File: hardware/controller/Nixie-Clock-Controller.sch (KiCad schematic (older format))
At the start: 62 parts, among them IC1 ESP32-DEVKITC-V4, IC2 74141, J1 9/12-35V DC in, J2 Nixies-Connector, J3 Buttons, J4 Buzzer, Q1 MPSA42, Q10 MPSA42, Q11 MPSA42, Q12 MPSA42, Q13 MPSA42, Q14 MPSA42, Q2 MPSA92, Q3 MPSA92, Q4 MPSA92, Q5 MPSA92, Q6 MPSA92, Q7 MPSA92, Q8 MPSA92, Q9 MPSA42, SW1 on/off, SW2 in voltage select, U1 L7805, U2 L7809, U3 NCH6300HV

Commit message: Add screw terminals for I/O, Improve PCB layout
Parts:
- removed D3: power-LED, LED_THT:LED_D5.0mm, symbol Device:LED
- removed J4: Buzzer, TerminalBlock_MetzConnect:TerminalBlock_MetzConnect_Type094_RT03502HBLU_1x02_P5.00mm_Horizontal, symbol Connector:Screw_Terminal_01x02
- removed R8: 100R, Resistor_THT:R_Axial_DIN0207_L6.3mm_D2.5mm_P10.16mm_Horizontal, symbol Device:R
- removed SW1: on/off, Button_Switch_THT:SW_E-Switch_EG1224_SPDT_Angled, symbol Switch:SW_SPDT
- removed SW2: in voltage select, Button_Switch_THT:SW_E-Switch_EG1224_SPDT_Angled, symbol Switch:SW_SPDT
- added J4: Output, TerminalBlock_RND:TerminalBlock_RND_205-00018_1x08_P5.00mm_Horizontal, symbol Connector:Screw_Terminal_01x08
- added J5: LEDs, TerminalBlock_RND:TerminalBlock_RND_205-00014_1x04_P5.00mm_Horizontal, symbol Connector:Screw_Terminal_01x04
- added R3: 220R, Resistor_THT:R_Axial_DIN0207_L6.3mm_D2.5mm_P10.16mm_Horizontal, symbol Device:R
- added SW1: on/off, TerminalBlock_RND:TerminalBlock_RND_205-00012_1x02_P5.00mm_Horizontal, symbol Connector:Screw_Terminal_01x02
- added SW2: in voltage select, TerminalBlock_RND:TerminalBlock_RND_205-00013_1x03_P5.00mm_Horizontal, symbol Connector:Screw_Terminal_01x03
- IC1: symbol ESP32-DEVKITC-32D:ESP32-DEVKITC-32D -> Nixie-Clock-Controller-rescue:ESP32-DEVKITC-32D-ESP32-DEVKITC-32D
- J1: footprint Connector_BarrelJack:BarrelJack_Horizontal -> TerminalBlock_RND:TerminalBlock_RND_205-00012_1x02_P5.00mm_Horizontal; symbol Connector:Barrel_Jack -> Connector:Screw_Terminal_01x02
- J3: value Buttons -> Input; footprint TerminalBlock_MetzConnect:TerminalBlock_MetzConnect_Type094_RT03506HBLU_1x06_P5.00mm_Horizontal -> TerminalBlock_RND:TerminalBlock_RND_205-00020_1x10_P5.00mm_Horizontal; symbol Connector:Screw_Terminal_01x06 -> Connector:Screw_Terminal_01x10
- U3: symbol nch6300hv:NCH6300HV -> Nixie-Clock-Controller-rescue:NCH6300HV-nch6300hv
- renumbered R32 to R10, R6 to R11, R15 to R12, R16 to R13, R17 to R14, R18 to R15, R19 to R16, R20 to R17, R7 to R18, R9 to R19, R5 to R2, R10 to R20, R11 to R21, R12 to R22, R13 to R23, R14 to R24, R21 to R25, R22 to R26, R23 to R27, R24 to R28, R25 to R29, R26 to R30, R27 to R5, R28 to R6, R29 to R7, R30 to R8, R31 to R9
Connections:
- net GND: now also J1.1 (Pin_1), J3.7 (Pin_7), J3.9 (Pin_9), J4.1 (Pin_1), J4.3 (Pin_3), J4.5 (Pin_5), J4.7 (Pin_7), J5.1 (Pin_1), J5.3 (Pin_3); no longer J1.2
- net b_reset: now also J3.10 (Pin_10); no longer J3.6 (Pin_6)
- net out_1: now reaches IC1.25 (IO21)
- net out_1: now also J4.8 (Pin_8)
- net at R2.2: now also J5.2 (Pin_2)
- net at C3.1, D2.1 (K), U3.1 (GND): now also SW2.3 (Pin_3)
- net at IC1.13 (IO12): now also R3.1
- net out_2: now reaches IC1.31 (IO16)
- net out_2: now also J4.6 (Pin_6)
- net out_3: now reaches IC1.32 (IO4)
- net out_3: now also J4.4 (Pin_4)
- net out_4: now reaches IC1.33 (IO0)
- net out_4: now also J4.2 (Pin_2)
- net in_3: now reaches IC1.5 (IO34)
- net in_3: now also J3.4 (Pin_4)
- net in_4: now reaches IC1.6 (IO35)
- net in_4: now also J3.2 (Pin_2)
- net at D1.2 (A): now also J1.2 (Pin_2); no longer J1.1
- net at C2.1, U1.1 (IN): now also SW1.1 (Pin_1), SW2.1 (Pin_1)
- net at D1.1 (K): now also SW1.2 (Pin_2)
- net at C4.1, U2.1 (IN): now also SW2.2 (Pin_2)
- net b_hour renamed in_1
- net in_1: now also J3.8 (Pin_8); no longer J3.4 (Pin_4)
- net b_min renamed in_2
- net in_2: now also J3.6 (Pin_6); no longer J3.2 (Pin_2)
- new net led_status: J5.4 (Pin_4), R3.2
- no-connect marks 23 -> 16
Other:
- moved on the sheet: J1

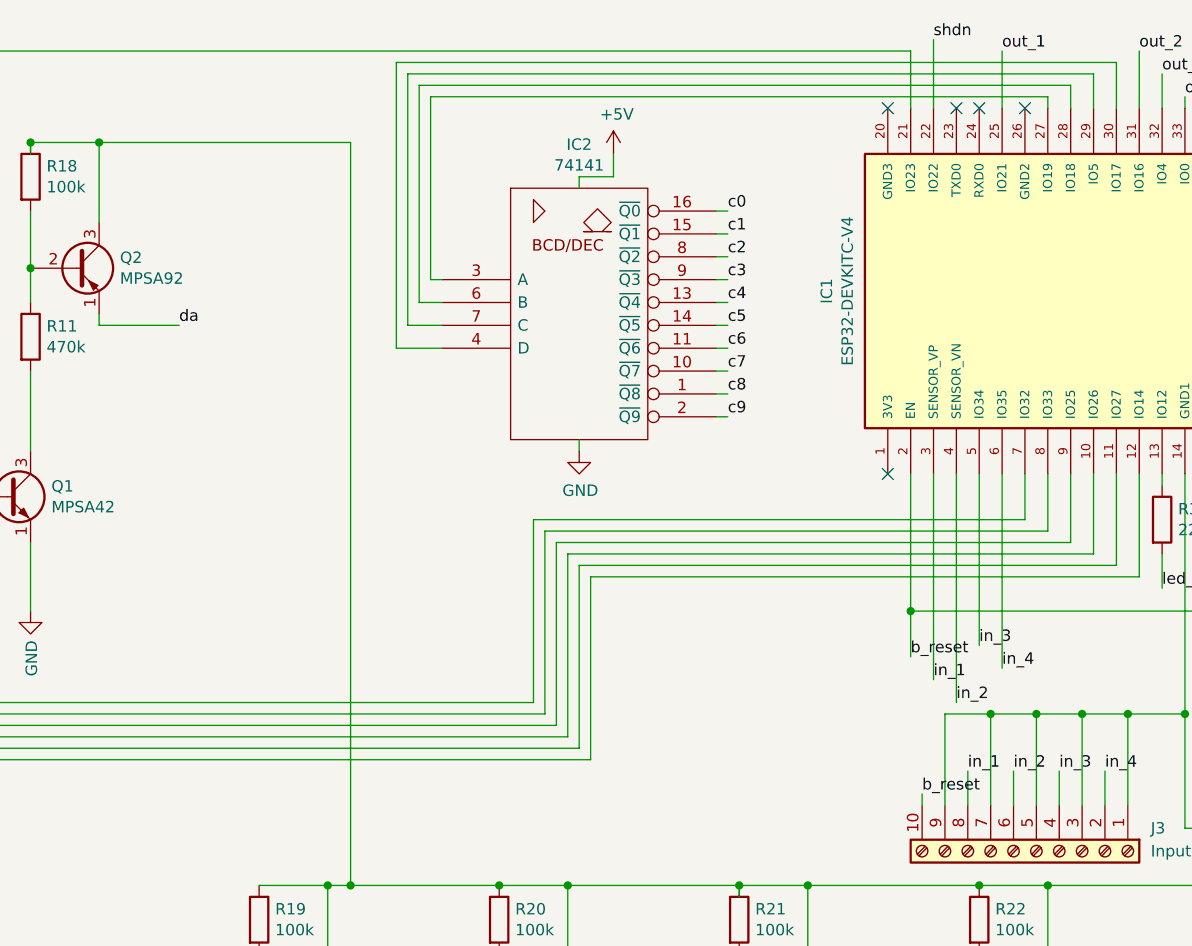
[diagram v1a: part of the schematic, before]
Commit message: Add Mounting Holes to PCB, Improve Routing, Add power pin header, Use correct connector footprint
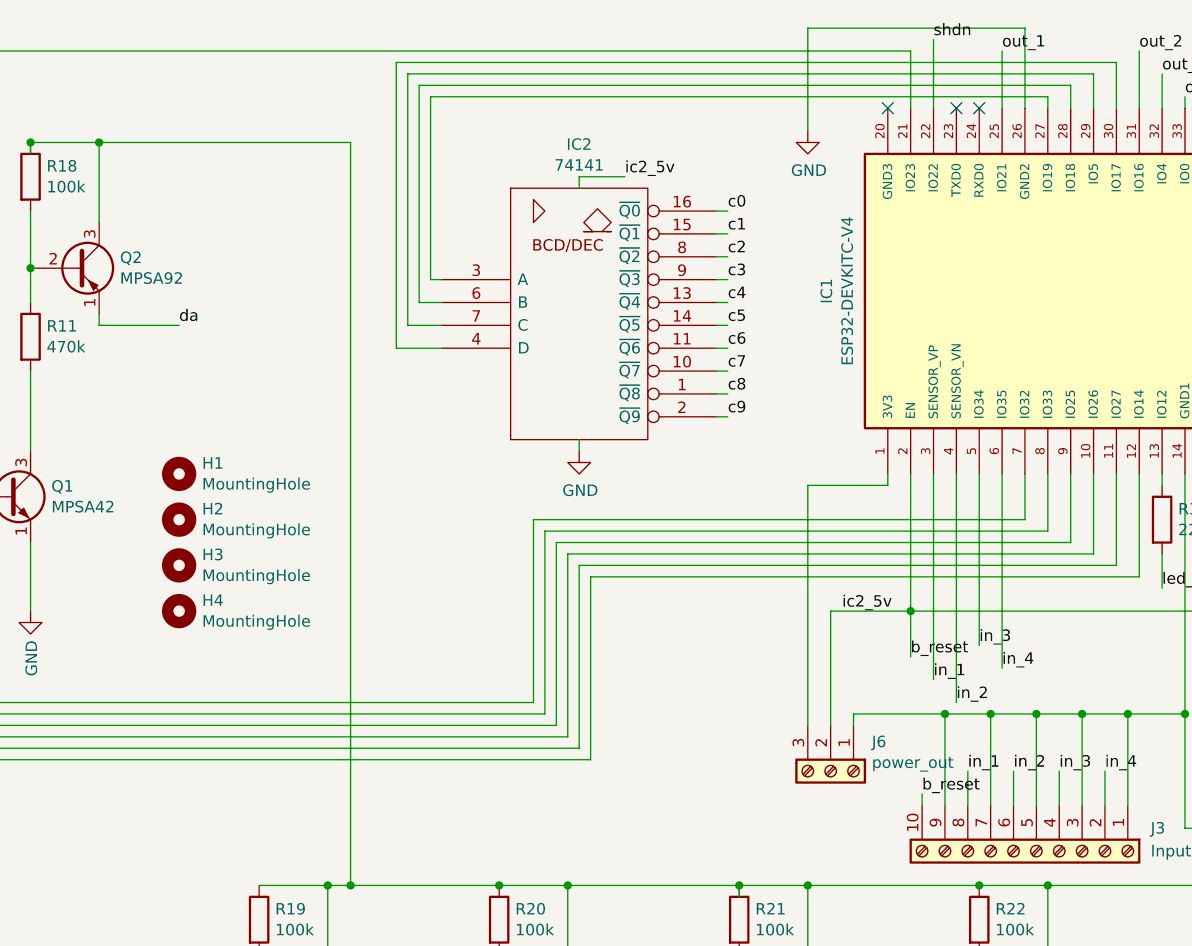
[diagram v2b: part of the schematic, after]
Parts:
- added H1, H2, H3, H4: MountingHole, MountingHole:MountingHole_2.7mm_M2.5, symbol Mechanical:MountingHole
- added J6: power_out, TerminalBlock_RND:TerminalBlock_RND_205-00013_1x03_P5.00mm_Horizontal, symbol Connector:Screw_Terminal_01x03
- J2: footprint Connector_PinHeader_2.54mm:PinHeader_2x10_P2.54mm_Horizontal -> nixie-clock:PinHeader_2x10_P2.54mm_Horizontal_with_Interlock
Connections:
- net b_reset is gone; now on net VCC: IC1.2 (EN), J3.10 (Pin_10), R1.2
- net GND: now also IC1.26 (GND2), J6.1 (Pin_1)
- net at IC1.1 (3V3): now also J6.3 (Pin_3)
- net +5V renamed VCC
- net VCC: now also J6.2 (Pin_2)
- no-connect marks 16 -> 14
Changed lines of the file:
@@
-$EndComp
-$Comp
-L power:+5V #PWR08
-U 1 1 619C404E
-P 3850 1050
-F 0 "#PWR08" H 3850 900 50  0001 C CNN
-F 1 "+5V" H 3865 1223 50  0000 C CNN
-F 2 "" H 3850 1050 50  0001 C CNN
-F 3 "" H 3850 1050 50  0001 C CNN
-	1    3850 1050
-	1    0    0    -1
 $EndComp
 $Comp
@@
 Wire Wire Line
 	5750 800  5750 850
-NoConn ~ 5050 2450
 Wire Wire Line
 	2900 650  6050 650
@@
 Wire Wire Line
 	2900 1900 2900 650
-Wire Wire Line
-	3700 1200 3700 1150
-Wire Wire Line
-	3700 1150 3850 1150
-Wire Wire Line
-	3850 1150 3850 1050
-NoConn ~ 5050 850
 NoConn ~ 6450 2450
 NoConn ~ 6450 850
 NoConn ~ 6550 850
-NoConn ~ 5650 850
 Wire Wire Line
 	8450 3850 8450 2250
@@
 F 0 "J2" V 9696 4862 50  0000 R CNN
 F 1 "Nixies-Connector" V 9605 4862 50  0000 R CNN
-F 2 "Connector_PinHeader_2.54mm:PinHeader_2x10_P2.54mm_Horizontal" H 9600 5450 50  0001 C CNN
+F 2 "nixie-clock:PinHeader_2x10_P2.54mm_Horizontal_with_Interlock" H 9600 5450 50  0001 C CNN
 F 3 "~" H 9600 5450 50  0001 C CNN
 	1    9600 5450
@@
 Wire Wire Line
 	10450 2500 10450 3300
+$Comp
+L Connector:Screw_Terminal_01x03 J6
+U 1 1 61CCA78D
+P 4800 3750
+F 0 "J6" V 4672 3930 50  0000 L CNN
+F 1 "power_out" V 4763 3930 50  0000 L CNN
+F 2 "TerminalBlock_RND:TerminalBlock_RND_205-00013_1x03_P5.00mm_Horizontal" H 4800 3750 50  0001 C CNN
+F 3 "~" H 4800 3750 50  0001 C CNN
+	1    4800 3750
+	0    1    1    0
+$EndComp
+Wire Wire Line
+	4900 3550 4900 3500
+Wire Wire Line
+	4900 3500 5300 3500
+Connection ~ 5300 3500
+Wire Wire Line
+	5150 3050 4800 3050
+Wire Wire Line
+	4800 3050 4800 3550
+Wire Wire Line
+	5050 2450 5050 2500
+Wire Wire Line
+	5050 2500 4700 2500
+Wire Wire Line
+	4700 2500 4700 3550
+Text Label 4850 3050 0    50   ~ 0
+ic2_5v
+Text Label 3900 1150 0    50   ~ 0
+ic2_5v
+Wire Wire Line
+	3900 1150 3700 1150
+Wire Wire Line
+	3700 1150 3700 1200
+$Comp
+L power:GND #PWR0103
+U 1 1 61EC4C44
+P 4700 950
+F 0 "#PWR0103" H 4700 700 50  0001 C CNN
+F 1 "GND" H 4705 777 50  0000 C CNN
+F 2 "" H 4700 950 50  0001 C CNN
+F 3 "" H 4700 950 50  0001 C CNN
+	1    4700 950
+	1    0    0    -1
+$EndComp
+Wire Wire Line
+	5650 850  5650 500
+Wire Wire Line
+	5650 500  4700 500
+$Comp
+L Mechanical:MountingHole H1
+U 1 1 61F780CD
+P 1950 2450
+F 0 "H1" H 2050 2496 50  0000 L CNN
+F 1 "MountingHole" H 2050 2405 50  0000 L CNN
+F 2 "MountingHole:MountingHole_2.7mm_M2.5" H 1950 2450 50  0001 C CNN
+F 3 "~" H 1950 2450 50  0001 C CNN
+	1    1950 2450
+	1    0    0    -1
+$EndComp
+$Comp
+L Mechanical:MountingHole H2
+U 1 1 61F7A90E
+P 1950 2650
+F 0 "H2" H 2050 2696 50  0000 L CNN
+F 1 "MountingHole" H 2050 2605 50  0000 L CNN
+F 2 "MountingHole:MountingHole_2.7mm_M2.5" H 1950 2650 50  0001 C CNN
+F 3 "~" H 1950 2650 50  0001 C CNN
+	1    1950 2650
+	1    0    0    -1
+$EndComp
+$Comp
+L Mechanical:MountingHole H3
+U 1 1 61F7B280
+P 1950 2850
+F 0 "H3" H 2050 2896 50  0000 L CNN
+F 1 "MountingHole" H 2050 2805 50  0000 L CNN
+F 2 "MountingHole:MountingHole_2.7mm_M2.5" H 1950 2850 50  0001 C CNN
+F 3 "~" H 1950 2850 50  0001 C CNN
+	1    1950 2850
+	1    0    0    -1
+$EndComp
+$Comp
+L Mechanical:MountingHole H4
+U 1 1 61F7BA05
+P 1950 3050
+F 0 "H4" H 2050 3096 50  0000 L CNN
+F 1 "MountingHole" H 2050 3005 50  0000 L CNN
+F 2 "MountingHole:MountingHole_2.7mm_M2.5" H 1950 3050 50  0001 C CNN
+F 3 "~" H 1950 3050 50  0001 C CNN
+	1    1950 3050
+	1    0    0    -1
+$EndComp
+Wire Wire Line
+	4700 500  4700 950
+NoConn ~ 5050 850
 $EndSCHEMATC

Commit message: Fix libraries used in Nixie-Clock-Controller
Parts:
- IC1: symbol Nixie-Clock-Controller-rescue:ESP32-DEVKITC-32D-ESP32-DEVKITC-32D -> nixie-clock:ESP32-DEVKITC-32D
- U3: symbol Nixie-Clock-Controller-rescue:NCH6300HV-nch6300hv -> nixie-clock:NCH6300HV
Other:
- moved on the sheet: H1, H2, H3, H4
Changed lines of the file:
@@
 encoding utf-8
 Sheet 1 1
-Title "Nixie-Clock-Control"
-Date "2021-12-22"
-Rev "ESP32 - 0.5"
-Comp "Konrad"
+Title "Nixie-Clock: Controller"
+Date "2021-12-25"
+Rev "1.0"
+Comp "Konrad Mösch"
 Comment1 ""
 Comment2 ""
@@
 NoConn ~ 6550 2450
 $Comp
-L Nixie-Clock-Controller-rescue:ESP32-DEVKITC-32D-ESP32-DEVKITC-32D IC1
+L nixie-clock:ESP32-DEVKITC-32D IC1
 U 1 1 61C74D2B
 P 5950 1650
@@
 NoConn ~ 10000 5150
 $Comp
-L Nixie-Clock-Controller-rescue:NCH6300HV-nch6300hv U3
+L nixie-clock:NCH6300HV U3
 U 1 1 61C726B5
 P 9400 3850
@@
 L Mechanical:MountingHole H1
 U 1 1 61F780CD
-P 1950 2450
-F 0 "H1" H 2050 2496 50  0000 L CNN
-F 1 "MountingHole" H 2050 2405 50  0000 L CNN
-F 2 "MountingHole:MountingHole_2.7mm_M2.5" H 1950 2450 50  0001 C CNN
-F 3 "~" H 1950 2450 50  0001 C CNN
-	1    1950 2450
+P 850 750
+F 0 "H1" H 950 796 50  0000 L CNN
+F 1 "MountingHole" H 950 705 50  0000 L CNN
+F 2 "MountingHole:MountingHole_2.7mm_M2.5" H 850 750 50  0001 C CNN
+F 3 "~" H 850 750 50  0001 C CNN
+	1    850  750
 	1    0    0    -1
 $EndComp
@@
 L Mechanical:MountingHole H2
 U 1 1 61F7A90E
-P 1950 2650
-F 0 "H2" H 2050 2696 50  0000 L CNN
-F 1 "MountingHole" H 2050 2605 50  0000 L CNN
-F 2 "MountingHole:MountingHole_2.7mm_M2.5" H 1950 2650 50  0001 C CNN
-F 3 "~" H 1950 2650 50  0001 C CNN
-	1    1950 2650
+P 10900 800
+F 0 "H2" H 11000 846 50  0000 L CNN
+F 1 "MountingHole" H 11000 755 50  0000 L CNN
+F 2 "MountingHole:MountingHole_2.7mm_M2.5" H 10900 800 50  0001 C CNN
+F 3 "~" H 10900 800 50  0001 C CNN
+	1    10900 800
 	1    0    0    -1
 $EndComp
@@
 L Mechanical:MountingHole H3
 U 1 1 61F7B280
-P 1950 2850
-F 0 "H3" H 2050 2896 50  0000 L CNN
-F 1 "MountingHole" H 2050 2805 50  0000 L CNN
-F 2 "MountingHole:MountingHole_2.7mm_M2.5" H 1950 2850 50  0001 C CNN
-F 3 "~" H 1950 2850 50  0001 C CNN
-	1    1950 2850
+P 850 7450
+F 0 "H3" H 950 7496 50  0000 L CNN
+F 1 "MountingHole" H 950 7405 50  0000 L CNN
+F 2 "MountingHole:MountingHole_2.7mm_M2.5" H 850 7450 50  0001 C CNN
+F 3 "~" H 850 7450 50  0001 C CNN
+	1    850  7450
 	1    0    0    -1
 $EndComp
@@
 L Mechanical:MountingHole H4
 U 1 1 61F7BA05
-P 1950 3050
-F 0 "H4" H 2050 3096 50  0000 L CNN
-F 1 "MountingHole" H 2050 3005 50  0000 L CNN
-F 2 "MountingHole:MountingHole_2.7mm_M2.5" H 1950 3050 50  0001 C CNN
-F 3 "~" H 1950 3050 50  0001 C CNN
-	1    1950 3050
-	1    0    0    -1
-$EndComp
+P 10900 6250
+F 0 "H4" H 11000 6296 50  0000 L CNN
+F 1 "MountingHole" H 11000 6205 50  0000 L CNN
+F 2 "MountingHole:MountingHole_2.7mm_M2.5" H 10900 6250 50  0001 C CNN
+F 3 "~" H 10900 6250 50  0001 C CNN
+	1    10900 6250
+	1    0    0    -1
+$EndComp
